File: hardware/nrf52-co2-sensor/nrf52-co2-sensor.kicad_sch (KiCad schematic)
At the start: 27 parts, among them J1 USB4105-GF-A, J2 SCD30, J3 Conn_01x02, J4 SWD, SW1 SW_Push, U1 USBLC6-2P6, U2 MDBT50Q-1MV2

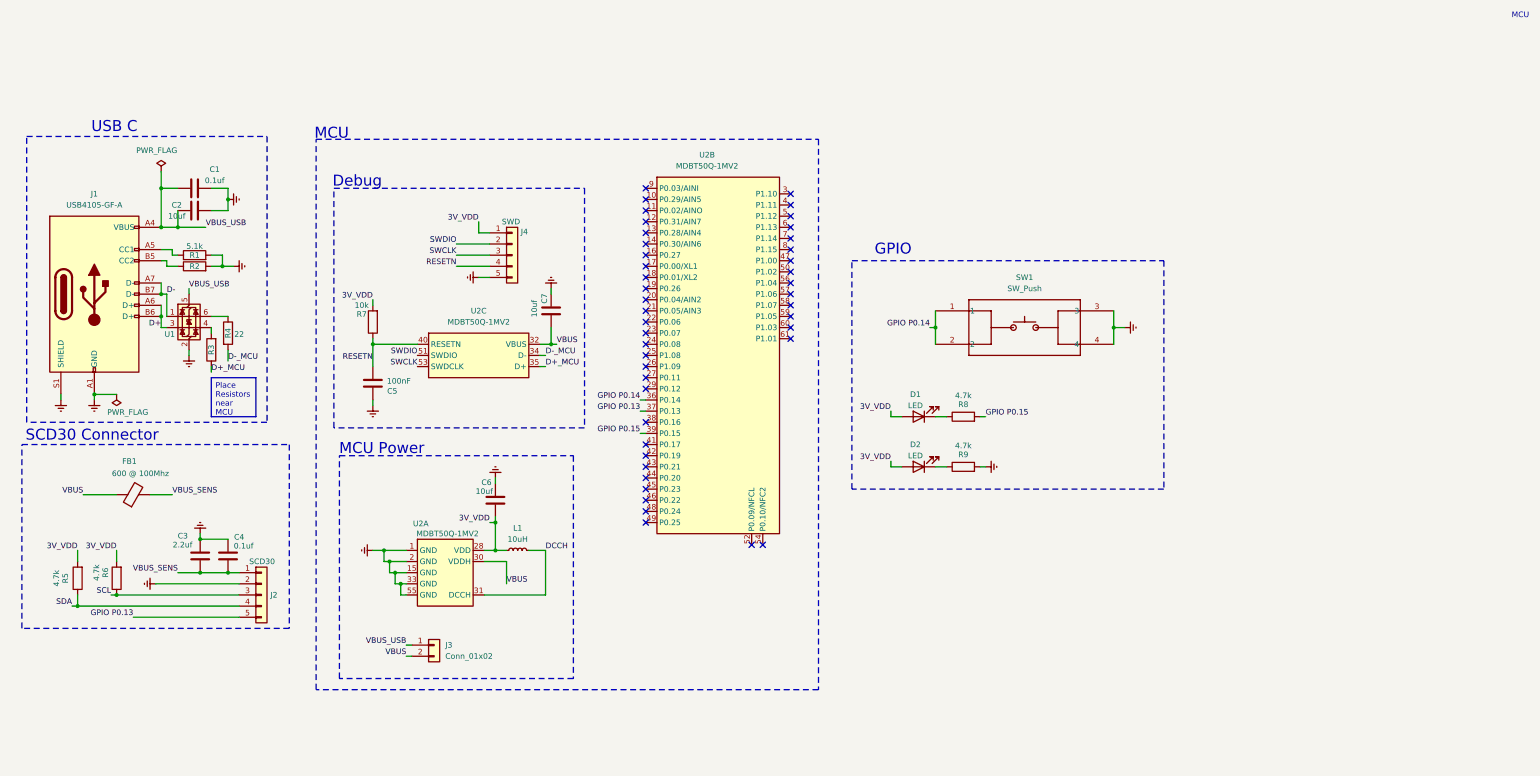
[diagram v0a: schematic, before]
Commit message: Changes made to schematic. BJT Lowpass filter, jumper for power measurement/choosing battery vs usb power, removal of redundant capacitors, and other additional fixes.
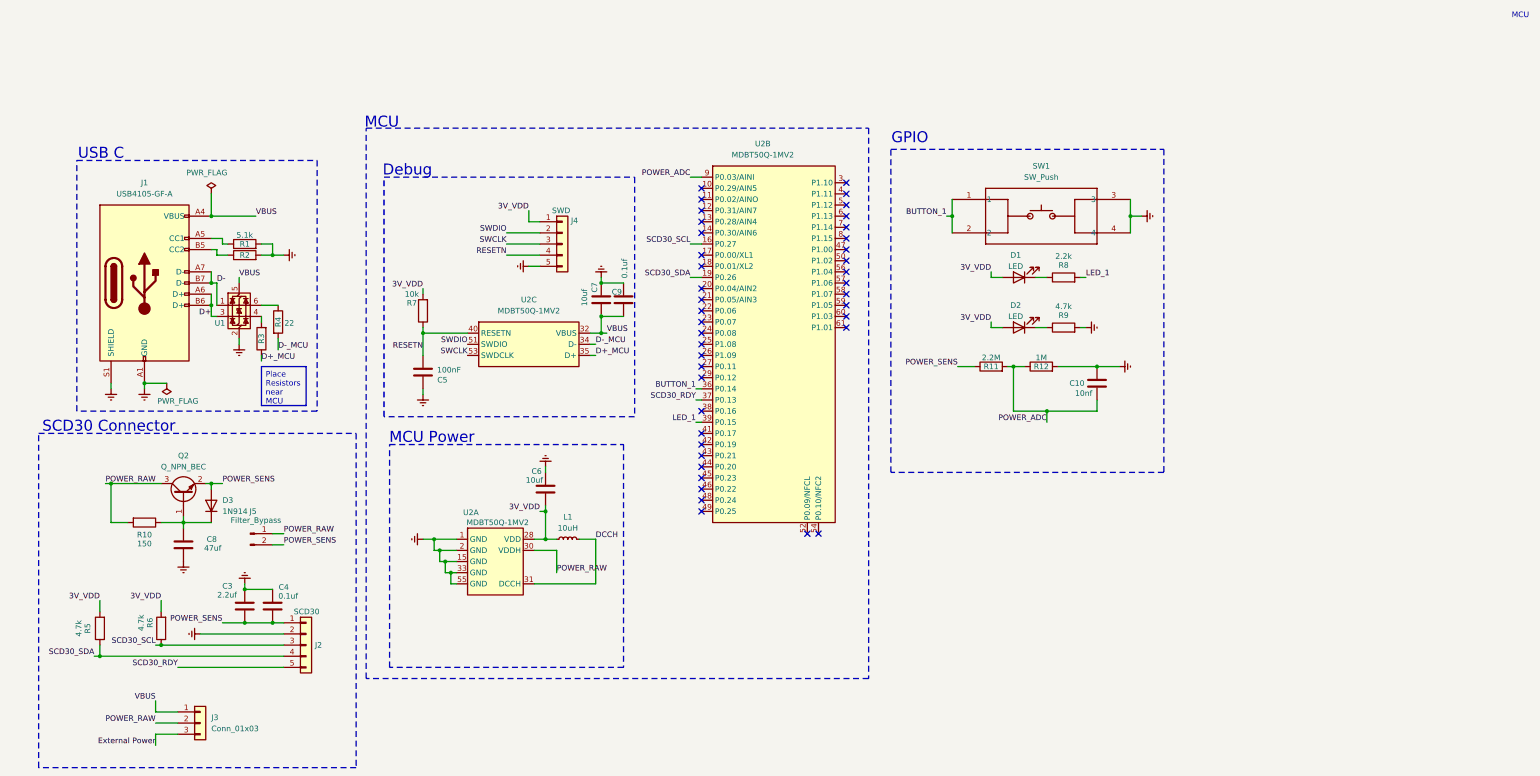
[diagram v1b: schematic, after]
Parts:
- removed C1: 0.1uf, Capacitor_SMD:C_0402_1005Metric, symbol Device:C
- removed C2: 10uf, Capacitor_SMD:C_0402_1005Metric, symbol Device:C
- removed FB1: 600 @ 100Mhz, nrf52-co2-sensor:BLM15AX601SN1D, symbol Device:FerriteBead
- removed J3: Conn_01x02, Connector_PinHeader_1.00mm:PinHeader_1x02_P1.00mm_Vertical, symbol Connector_Generic:Conn_01x02
- added C10: 10nf, Capacitor_SMD:C_0402_1005Metric, symbol Device:C
- added C8: 47uf, Capacitor_SMD:C_0402_1005Metric, symbol Device:C
- added C9: 0.1uf, Capacitor_SMD:C_0402_1005Metric, symbol Device:C
- added D3: 1N914, Diode_THT:D_DO-35_SOD27_P7.62mm_Horizontal, symbol Diode:1N914
- added J3: Conn_01x03, symbol Connector_Generic:Conn_01x03
- added J5: Filter_Bypass, symbol Connector:Conn_01x02_Pin
- added Q2: Q_NPN_BEC, symbol Transistor_BJT:Q_NPN_BEC
- added R10: 150, Resistor_SMD:R_0402_1005Metric, symbol Device:R
- added R11: 2.2M, Resistor_SMD:R_0402_1005Metric, symbol Device:R
- added R12: 1M, Resistor_SMD:R_0402_1005Metric, symbol Device:R
- R8: value 4.7k -> 2.2k
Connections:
- net SCL is gone; now on net SCD30_SCL: J2.3 (Pin_3), R6.1
- net SDA is gone; now on net SCD30_SDA: J2.4 (Pin_4), R5.1
- net VBUS_USB is gone; now on net VBUS: J1.A4 (VBUS), J1.A9 (VBUS), J1.B4 (VBUS), J1.B9 (VBUS), U1.5 (VBUS)
- net GND: now also C10.1, C8.1, C9.2, R12.2
- net VBUS: now also C9.1, J3.1 (Pin_1); no longer U2.30 (VDDH)
- net SCD30_SCL: now reaches U2.16 (P0.27)
- net SCD30_SDA: now reaches U2.19 (P0.26)
- net POWER_ADC: now reaches U2.9 (P0.03/AINI)
- net POWER_ADC: now also C10.2, R11.2, R12.1
- net GPIO P0.13 renamed SCD30_RDY
- net GPIO P0.14 renamed BUTTON_1
- net GPIO P0.15 renamed LED_1
- net VBUS_SENS renamed POWER_SENS
- net POWER_SENS: now also D3.2 (A), J5.2 (Pin_2), Q2.2 (E), R11.1
- new net: C8.2, D3.1 (K), Q2.1 (B), R10.1
- new net External Power: J3.3 (Pin_3)
- new net POWER_RAW: J3.2 (Pin_2), J5.1 (Pin_1), Q2.3 (C), R10.2, U2.30 (VDDH)
- no-connect marks 44 -> 41
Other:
- moved on the sheet: C3, C4, C5, C6, C7, D1, D2, J1, J2, J4, L1, R1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
